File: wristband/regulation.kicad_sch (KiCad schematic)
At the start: 3 parts, among them U5 MCP1700T-3302E/TT

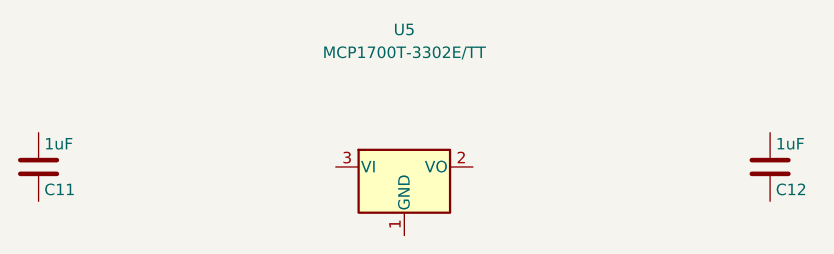
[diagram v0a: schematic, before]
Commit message: Migrate wristband to NINA-B400, wire all sheets, close six design gaps
Replaces the wristband's u-blox NINA-B111 (nRF52832) with a NINA-B400-00B
(Nordic nRF52833, Bluetooth 5.1), then follows through on everything that
change and a full schematic review surfaced.

NINA-B400 migration
- New 55-pin + EGP + EAGP symbol, transcribed from the real NINA-B40 data
  sheet UBX-19049405 R09 Table 6 and cross-checked against Figure 3 for rank
  ordering. Pin numbering validated programmatically (1-55, each exactly once).
- NINA-B4 is pin/mechanically compatible with NINA-B3, NOT NINA-B1, so the
  42-pad NINA111-42 land pattern does not carry over. No official footprint
  exists anywhere -- u-blox's own Eagle library ships only NINA111-42/112-42,
  and neither KiCad's bundled nor upstream RF_Module library has a B3/B4 part.
  NINA-B400-55_PLACEHOLDER is therefore flagged: outline, pad count and rank
  arrangement are confirmed; individual pad X/Y are derived estimates.
  MUST be replaced before fabrication.
- B400 chosen over B401/B406 for its on-module U.FL connector, which let the
  PCB-side U.FL (J2) and the untuned L/C match network (L1/C13) be deleted --
  retiring the project's only open RF-tuning risk.
- No power-design impact: abs-max VCC is 3.9 V on both modules, so the MCP1700
  LDO rationale stands. Budget 12 mA -> 15.5 mA typ; ~70.5 mA with DWM3000
  against 250 mA, ~3.5x headroom (corrects a stale "3.7x" in the docs).
- SWD pin numbers are unchanged (SWDCLK=11, SWDIO=15, RESET_N=19, SWO=8).

Antenna re-verified, part number corrected
- The specified antenna is still pre-approved for NINA-B4 (certification app
  note UBX-20037320 R05 s3.2) but ProAnt was acquired by Abracon and u-blox
  now lists it as PRO-IS-237. Same specs throughout. Order under the Abracon PN.

Six gaps closed
- Y1 + C14/C15: 32.768 kHz LFXO (Epson FC-135, Q13FC13500004). Required for
  lowest sleep current per SIM UBX-19052230 R13 s1.9; XL1/XL2 were floating,
  which Table 6 does not permit eve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
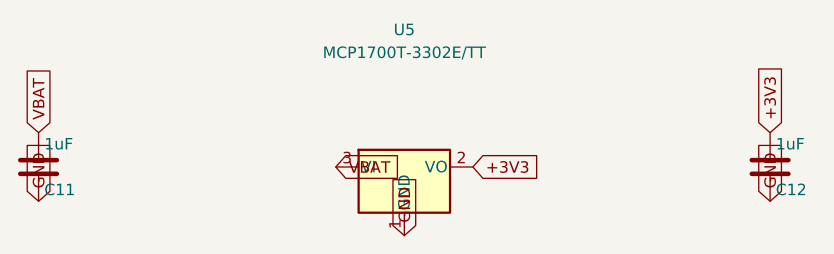
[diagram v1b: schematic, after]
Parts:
- C11, C12: MPN (none) -> CL10B105KA8NNNC; Manufacturer (none) -> Samsung Electro-Mechanics
- U5: MPN (none) -> MCP1700T-3302E/TT; Manufacturer (none) -> Microchip
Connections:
- net +3V3: now reaches C12.1
- net +3V3: now also U5.2 (VO)
- net GND: now reaches C12.2
- net GND: now also C11.2, U5.1 (GND)
- net VBAT: now reaches U5.3 (VI)
- net VBAT: now also C11.1
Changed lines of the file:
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@@
 	(title_block
 		(title "Regulation")
-		(comment 1 "Wristband VBAT (up to 4.2V) -> +3V3 LDO rail for NINA-B111 (abs max VCC 3.9V) and DWM3000 (abs max VDD3V3 4.0V) -- placement only, not yet wired")
+		(comment 1 "Wristband VBAT (up to 4.2V) -> +3V3 LDO rail for NINA-B400 (abs max VCC 3.9V) and DWM3000 (abs max VDD3V3 4.0V) -- placement only, not yet wired")
 	)
 	(symbol
@@
 			)
 		)
+		(property "MPN" "MCP1700T-3302E/TT"
+			(at 101.6 60.96 0)
+			(effects
+				(font
+					(size 1.27 1.27)
+				)
+				(hide yes)
+			)
+		)
+		(property "Manufacturer" "Microchip"
+			(at 101.6 60.96 0)
+			(effects
+				(font
+					(size 1.27 1.27)
+				)
+				(hide yes)
+			)
+		)
 		(pin "1"
 		)
@@
 			)
 		)
+		(property "MPN" "CL10B105KA8NNNC"
+			(at 61.595 78.74 0)
+			(effects
+				(font
+					(size 1.27 1.27)
+				)
+				(hide yes)
+			)
+		)
+		(property "Manufacturer" "Samsung Electro-Mechanics"
+			(at 61.595 78.74 0)
+			(effects
+				(font
+					(size 1.27 1.27)
+				)
+				(hide yes)
+			)
+		)
 		(pin "1"
 		)
@@
 			)
 		)
+		(property "MPN" "CL10B105KA8NNNC"
+			(at 142.875 78.74 0)
+			(effects
+				(font
+					(size 1.27 1.27)
+				)
+				(hide yes)
+			)
+		)
+		(property "Manufacturer" "Samsung Electro-Mechanics"
+			(at 142.875 78.74 0)
+			(effects
+				(font
+					(size 1.27 1.27)
+				)
+				(hide yes)
+			)
+		)
 		(pin "1"
 		)
@@
 		)
 	)
+	(global_label "GND"
+		(shape input)
+		(at 101.6 83.82 270)
+		(effects
+			(font
+				(size 1.27 1.27)
+			)
+			(justify left)
+		)
+	)
+	(global_label "+3V3"
+		(shape input)
+		(at 109.22 76.2 0)
+		(effects
+			(font
+				(size 1.27 1.27)
+			)
+			(justify left)
+		)
+	)
+	(global_label "VBAT"
+		(shape input)
+		(at 93.98 76.2 180)
+		(effects
+			(font
+				(size 1.27 1.27)
+			)
+			(justify left)
+		)
+	)
+	(global_label "VBAT"
+		(shape input)
+		(at 60.96 72.39 90)
+		(effects
+			(font
+				(size 1.27 1.27)
+			)
+			(justify left)
+		)
+	)
+	(global_label "GND"
+		(shape input)
+		(at 60.96 80.01 270)
+		(effects
+			(font
+				(size 1.27 1.27)
+			)
+			(justify left)
+		)
+	)
+	(global_label "+3V3"
+		(shape input)
+		(at 142.24 72.39 90)
+		(effects
+			(font
+				(size 1.27 1.27)
+			)
+			(justify left)
+		)
+	)
+	(global_label "GND"
+		(shape input)
+		(at 142.24 80.01 270)
+		(effects
+			(font
+				(size 1.27 1.27)
+			)
+			(justify left)
+		)
+	)

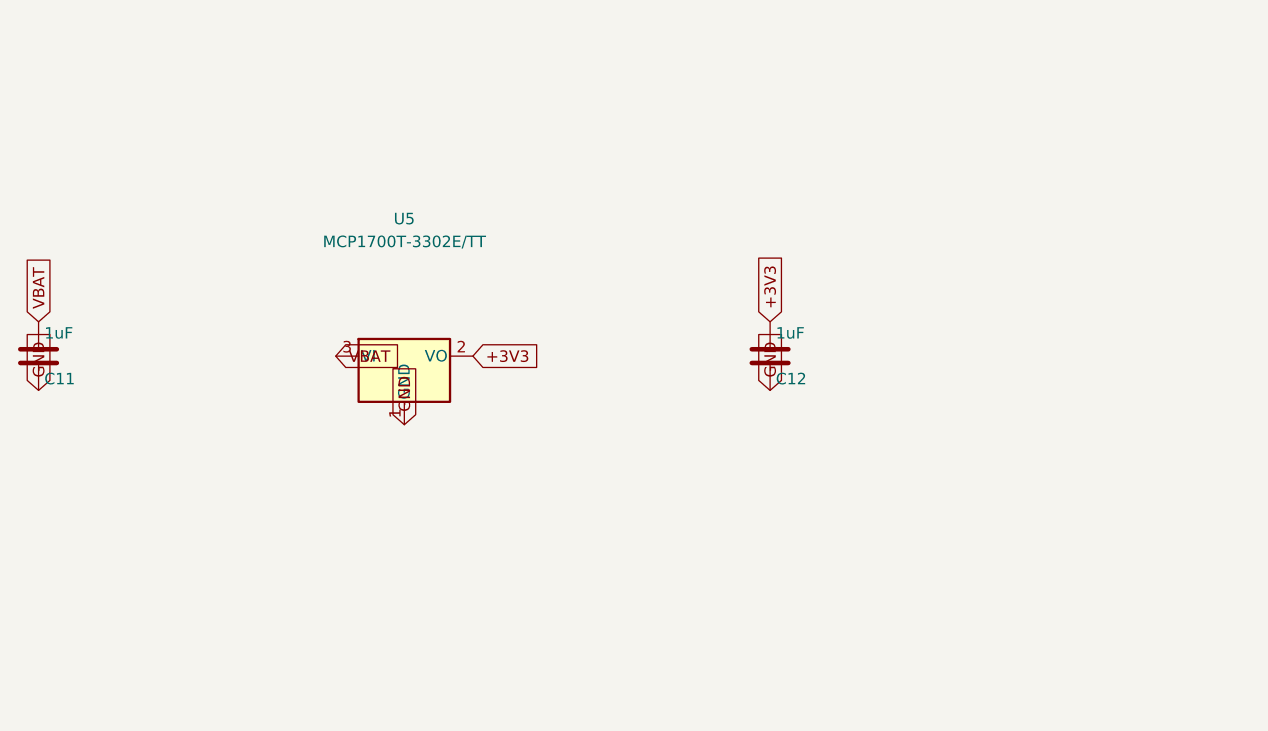
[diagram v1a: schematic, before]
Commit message: Make schematics readable: wire stubs, A3 reflow, DWM3000 symbol redraw
Connectivity is unchanged -- verified by diffing the exported netlist against
the previous commit: 34 nets, identical pin membership on every one. This is
presentation only.

The problem was pre-existing, not new. Labels were placed exactly on the pin
endpoint, so label text printed on top of the symbol's own pin name (+3V3
stamped over VCC, UWB_CS over GPIO_1). power_bms had it on U1/U2/Q2 as well;
it only became obvious when the convention was scaled onto a 55-pin part.
Every label now sits at the end of a short wire stub pointing away from the
body, which is the standard KiCad idiom.

DWM3000 symbol redrawn (shared/symbols/)
- The old symbol was a 20mm square carrying pin names like GPIO0/RXOKLED drawn
  vertically along the bottom edge, where they collided with each other inside
  the symbol. No amount of label placement fixes that.
- Now 56 x 41mm, functionally grouped: power/ground/control left, SPI/GPIO
  right, no bottom-edge pins. All 24 pins and every property preserved.
- Checked the blast radius before touching it: bay-station is entirely unwired
  (0 wires, 0 labels on every sheet), so nothing was orphaned. Its cached copy
  is refreshed here and its netlist still exports cleanly at 75 components.

Layout
- radio_mcu and power_bms moved to A3 and reflowed into functional blocks;
  42 symbols repositioned.
- 38 annotations added, carrying the datasheet citations and reasoning that
  previously lived only in the markdown -- LFXO load-cap derivation, the
  ~2.1uA battery-divider tradeoff, why DW01A's GND sits on CELL_N, the LDO
  headroom budget, and the unchanged-from-NINA-B111 SWD pin numbers.

Verification
- Wrote a text-collision checker rather than eyeballing it. It caught two
  classes of bug: duplicated annotations (strip() cleared labels and wires but
  not text, so a second pass layered notes over old ones) and doubled labels on
  stacked same-net pins (USB-C J1 A9/B9, A12/B12;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
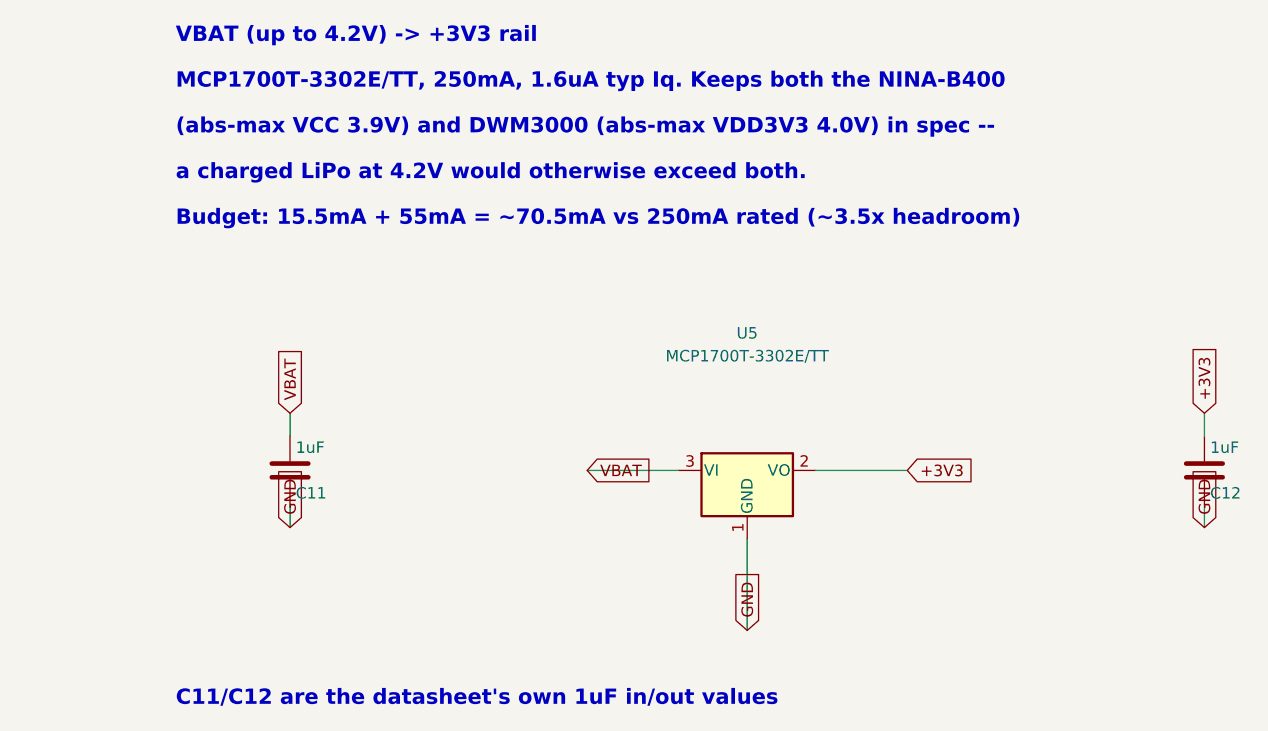
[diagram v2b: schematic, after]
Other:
- note added: "(abs-max VCC 3.9V) and DWM3000 (abs-max VDD3V3 4.0V) in spec --"
- note added: "Budget: 15.5mA + 55mA = ~70.5mA vs 250mA rated (~3.5x headroom)"
- note added: "C11/C12 are the datasheet's own 1uF in/out values"
- note added: "MCP1700T-3302E/TT, 250mA, 1.6uA typ Iq. Keeps both the NINA-B400"
- note added: "VBAT (up to 4.2V) -> +3V3 rail"
- note added: "a charged LiPo at 4.2V would otherwise exceed both."
- moved on the sheet: C11, C12, U5
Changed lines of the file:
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@@
 	(symbol
 		(lib_id "Regulator_Linear:MCP1700x-330xxTT")
-		(at 101.6 76.2 0)
+		(at 139.7 88.9 0)
 		(unit 1)
 		(exclude_from_sim no)
@@
 		(dnp no)
 		(property "Reference" "U5"
-			(at 101.6 60.96 0)
+			(at 139.7 73.66 0)
 			(effects
 				(font
@@
 		)
 		(property "Value" "MCP1700T-3302E/TT"
-			(at 101.6 63.5 0)
+			(at 139.7 76.2 0)
 			(effects
 				(font
@@
 		)
 		(property "Footprint" "Package_TO_SOT_SMD:SOT-23"
-			(at 101.6 76.2 0)
+			(at 139.7 88.9 0)
 			(effects
 				(font
@@
 		)
 		(property "Datasheet" ""
-			(at 101.6 76.2 0)
+			(at 139.7 88.9 0)
 			(effects
 				(font
@@
 		)
 		(property "MPN" "MCP1700T-3302E/TT"
-			(at 101.6 60.96 0)
+			(at 139.7 73.66 0)
 			(effects
 				(font
@@
 		)
 		(property "Manufacturer" "Microchip"
-			(at 101.6 60.96 0)
+			(at 139.7 73.66 0)
 			(effects
 				(font
@@
 	(symbol
 		(lib_id "Device:C")
-		(at 60.96 76.2 0)
+		(at 88.9 88.9 0)
 		(unit 1)
 		(exclude_from_sim no)
@@
 		(dnp no)
 		(property "Reference" "C11"
-			(at 61.595 78.74 0)
+			(at 89.535 91.44 0)
 			(effects
 				(font
@@
 		)
 		(property "Value" "1uF"
-			(at 61.595 73.66 0)
+			(at 89.535 86.36 0)
 			(effects
 				(font
@@
 		)
 		(property "Footprint" "Capacitor_SMD:C_0603_1608Metric"
-			(at 60.96 76.2 0)
+			(at 88.9 88.9 0)
 			(effects
 				(font
@@
 		)
 		(property "Datasheet" ""
-			(at 60.96 76.2 0)
+			(at 88.9 88.9 0)
 			(effects
 				(font
@@
 		)
 		(property "MPN" "CL10B105KA8NNNC"
-			(at 61.595 78.74 0)
+			(at 89.535 91.44 0)
 			(effects
 				(font
@@
 		)
 		(property "Manufacturer" "Samsung Electro-Mechanics"
-			(at 61.595 78.74 0)
+			(at 89.535 91.44 0)
 			(effects
 				(font
@@
 	(symbol
 		(lib_id "Device:C")
-		(at 142.24 76.2 0)
+		(at 190.5 88.9 0)
 		(unit 1)
 		(exclude_from_sim no)
@@
 		(dnp no)
 		(property "Reference" "C12"
-			(at 142.875 78.74 0)
+			(at 191.135 91.44 0)
 			(effects
 				(font
@@
 		)
 		(property "Value" "1uF"
-			(at 142.875 73.66 0)
+			(at 191.135 86.36 0)
 			(effects
 				(font
@@
 		)
 		(property "Footprint" "Capacitor_SMD:C_0603_1608Metric"
-			(at 142.24 76.2 0)
+			(at 190.5 88.9 0)
 			(effects
 				(font
@@
 		)
 		(property "Datasheet" ""
-			(at 142.24 76.2 0)
+			(at 190.5 88.9 0)
 			(effects
 				(font
@@
 		)
 		(property "MPN" "CL10B105KA8NNNC"
-			(at 142.875 78.74 0)
+			(at 191.135 91.44 0)
 			(effects
 				(font
@@
 		)
 		(property "Manufacturer" "Samsung Electro-Mechanics"
-			(at 142.875 78.74 0)
+			(at 191.135 91.44 0)
 			(effects
 				(font
@@
 		)
 	)
+	(wire
+		(pts
+			(xy 139.7 96.52) (xy 139.7 106.68)
+		)
+		(stroke
+			(width 0)
+			(type default)
+		)
+	)
 	(global_label "GND"
 		(shape input)
-		(at 101.6 83.82 270)
-		(effects
-			(font
-				(size 1.27 1.27)
-			)
-			(justify left)
+		(at 139.7 106.68 270)
+		(effects
+			(font
+				(size 1.27 1.27)
+			)
+			(justify left)
+		)
+	)
+	(wire
+		(pts
+			(xy 147.32 88.9) (xy 157.48 88.9)
+		)
+		(stroke
+			(width 0)
+			(type default)
 		)
 	)
 	(global_label "+3V3"
 		(shape input)
-		(at 109.22 76.2 0)
-		(effects
-			(font
-				(size 1.27 1.27)
-			)
-			(justify left)
+		(at 157.48 88.9 0)
+		(effects
+			(font
+				(size 1.27 1.27)
+			)
+			(justify left)
+		)
+	)
+	(wire
+		(pts
+			(xy 132.08 88.9) (xy 121.92 88.9)
+		)
+		(stroke
+			(width 0)
+			(type default)
 		)
 	)
 	(global_label "VBAT"
 		(shape input)
-		(at 93.98 76.2 180)
-		(effects
-			(font
-				(size 1.27 1.27)
-			)
-			(justify left)
+		(at 121.92 88.9 180)
+		(effects
+			(font
+				(size 1.27 1.27)
+			)
+			(justify left)
+		)
+	)
+	(wire
+		(pts
+			(xy 88.9 85.09) (xy 88.9 82.55)
+		)
+		(stroke
+			(width 0)
+			(type default)
 		)
 	)
 	(global_label "VBAT"
 		(shape input)
-		(at 60.96 72.39 90)
-		(effects
-			(font
-				(size 1.27 1.27)
-			)
-			(justify left)
+		(at 88.9 82.55 90)
+		(effects
+			(font
+				(size 1.27 1.27)
+			)
+			(justify left)
+		)
+	)
+	(wire
+		(pts
+			(xy 88.9 92.71) (xy 88.9 95.25)
+		)
+		(stroke
+			(width 0)
+			(type default)
 		)
 	)
 	(global_label "GND"
 		(shape input)
-		(at 60.96 80.01 270)
-		(effects
-			(font
-				(size 1.27 1.27)
-			)
-			(justify left)
+		(at 88.9 95.25 270)
+		(effects
+			(font
+				(size 1.27 1.27)
+			)
+			(justify left)
+		)
+	)
+	(wire
+		(pts
+			(xy 190.5 85.09) (xy 190.5 82.55)
+		)
+		(stroke
+			(width 0)
+			(type default)
 		)
 	)
 	(global_label "+3V3"
 		(shape input)
-		(at 142.24 72.39 90)
-		(effects
-			(font
-				(size 1.27 1.27)
-			)
-			(justify left)
+		(at 190.5 82.55 90)
+		(effects
+			(font
+				(size 1.27 1.27)
+			)
+			(justify left)
+		)
+	)
+	(wire
+		(pts
+			(xy 190.5 92.71) (xy 190.5 95.25)
+		)
+		(stroke
+			(width 0)
+			(type default)
 		)
 	)
 	(global_label "GND"
 		(shape input)
-		(at 142.24 80.01 270)
-		(effects
-			(font
-				(size 1.27 1.27)
-			)
-			(justify left)
+		(at 190.5 95.25 270)
+		(effects
+			(font
+				(size 1.27 1.27)
+			)
+			(justify left)
+		)
+	)
+	(text "VBAT (up to 4.2V) -> +3V3 rail"
+		(at 76.2 40.64 0)
+		(effects
+			(font
+				(size 1.7 1.7)
+				(bold yes)
+			)
+			(justify left)
+		)
+	)
+	(text "MCP1700T-3302E/TT, 250mA, 1.6uA typ Iq. Keeps both the NINA-B400"
+		(at 76.2 45.72 0)
+		(effects
+			(font
+				(size 1.7 1.7)
+				(bold yes)
+			)
+			(justify left)
+		)
+	)
+	(text "(abs-max VCC 3.9V) and DWM3000 (abs-max VDD3V3 4.0V) in spec --"
+		(at 76.2 50.8 0)
+		(effects
+			(font
+				(size 1.7 1.7)
+				(bold yes)
+			)
+			(justify left)
+		)
+	)
+	(text "a charged LiPo at 4.2V would otherwise exceed both."
+		(at 76.2 55.88 0)
+		(effects
+			(font
+				(size 1.7 1.7)
+				(bold yes)
+			)
+			(justify left)
+		)
+	)
+	(text "Budget: 15.5mA + 55mA = ~70.5mA vs 250mA rated (~3.5x headroom)"
+		(at 76.2 60.96 0)
+		(effects
+			(font
+				(size 1.7 1.7)
+				(bold yes)
+			)
+			(justify left)
+		)
+	)
+	(text "C11/C12 are the datasheet's own 1uF in/out values"
+		(at 76.2 114.3 0)
+		(effects
+			(font
+				(size 1.7 1.7)
+				(bold yes)
+			)
+			(justify left)
